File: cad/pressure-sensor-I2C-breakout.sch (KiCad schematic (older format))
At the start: 9 parts, among them P1 CONN_4, P2 CONN_4, U1 MPXV-PRESSURE-SENSOR, U2 LTC2483

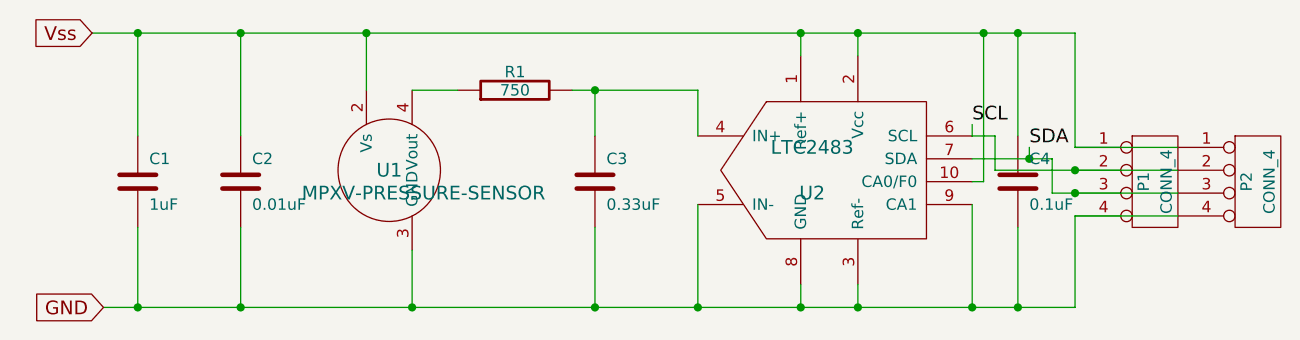
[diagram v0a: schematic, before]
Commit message: Fixing broken heater logic. Clunky but obvious code
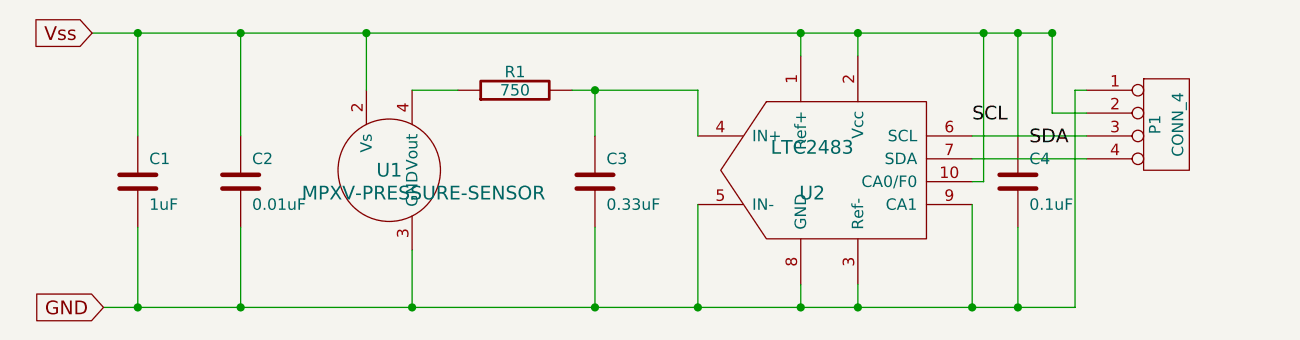
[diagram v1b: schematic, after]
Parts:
- removed P2: CONN_4, symbol CONN_4
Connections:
- net GND: now also P1.1 (P1); no longer P1.4 (P4)
- net SCL: no longer P1.2 (P2), U2.6 (SCL)
- net SDA: no longer P1.3 (P3), U2.7 (SDA)
- net Vss: now also P1.2 (P2); no longer P1.1 (P1)
- new net: P1.3 (P3), U2.6 (SCL)
- new net: P1.4 (P4), U2.7 (SDA)
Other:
- moved on the sheet: P1
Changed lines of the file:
@@
-EESchema Schematic File Version 2  date Mon 24 Feb 2014 17:03:24 NZDT
+EESchema Schematic File Version 2
 LIBS:power
 LIBS:device
@@
 LIBS:valves
 LIBS:state-machine-library_kicad
-EELAYER 25  0
+LIBS:pressure-sensor-I2C-breakout-cache
+EELAYER 27 0
 EELAYER END
-$Descr A4 11700 8267
+$Descr A4 11693 8268
 encoding utf-8
 Sheet 1 1
 Title ""
-Date "23 feb 2014"
+Date "20 may 2014"
 Rev ""
 Comp ""
@@
 Wire Wire Line
 	7250 2850 7200 2850
-Connection ~ 7450 2750
-Wire Wire Line
-	7450 2700 7450 2750
 Connection ~ 3550 3400
 Wire Wire Line
@@
 	4750 2450 4950 2450
 Wire Wire Line
-	8100 2900 7550 2900
-Wire Wire Line
-	7550 2900 7550 2750
-Wire Wire Line
-	7550 2750 7200 2750
+	7200 2750 7700 2750
 Connection ~ 6700 2200
 Wire Wire Line
-	6700 2300 6700 2200
+	6700 2200 6700 2300
 Connection ~ 6700 3400
 Wire Wire Line
@@
 Wire Wire Line
 	6000 2950 6000 3400
-Wire Wire Line
-	8100 2700 7650 2700
-Connection ~ 7650 2900
 Connection ~ 7400 2200
 Wire Wire Line
@@
 Connection ~ 4000 2200
 Wire Wire Line
-	4000 2650 4000 2200
+	4000 2200 4000 2650
 Connection ~ 4000 3400
 Wire Wire Line
@@
 Wire Wire Line
 	3550 3400 3550 3050
-Wire Wire Line
-	7650 3400 7650 3000
-Wire Wire Line
-	7650 2700 7650 2200
 Wire Wire Line
 	3550 2200 3550 2650
@@
 Connection ~ 7400 3400
 Wire Wire Line
-	7650 3000 8100 3000
-Connection ~ 7650 2800
-Wire Wire Line
 	5450 2450 6000 2450
 Wire Wire Line
@@
 Connection ~ 6450 3400
 Wire Wire Line
-	6450 2300 6450 2200
+	6450 2200 6450 2300
 Connection ~ 6450 2200
 Wire Wire Line
-	7300 2650 7200 2650
-Wire Wire Line
-	7300 2650 7300 2800
-Wire Wire Line
-	7300 2800 8100 2800
+	7200 2650 7700 2650
 Wire Wire Line
 	4550 2200 4550 2450
 Wire Wire Line
 	4750 3150 4750 3400
-Wire Wire Line
-	7650 2200 3350 2200
 Connection ~ 3550 2200
-Wire Wire Line
-	7200 2650 7200 2600
 Wire Wire Line
 	7200 2950 7200 3400
@@
 GND
 $Comp
-L CONN_4 P2
-U 1 1 530999F2
-P 8450 2850
-F 0 "P2" V 8400 2850 50  0000 C CNN
-F 1 "CONN_4" V 8500 2850 50  0000 C CNN
-	1    8450 2850
-	1    0    0    -1
-$EndComp
-$Comp
 L CONN_4 P1
 U 1 1 530997F9
-P 8000 2850
-F 0 "P1" V 7950 2850 50  0000 C CNN
-F 1 "CONN_4" V 8050 2850 50  0000 C CNN
-	1    8000 2850
+P 8050 2600
+F 0 "P1" V 8000 2600 50  0000 C CNN
+F 1 "CONN_4" V 8100 2600 50  0000 C CNN
+F 2 "" H 8050 2600 60  0001 C CNN
+F 3 "" H 8050 2600 60  0001 C CNN
+	1    8050 2600
 	1    0    0    -1
 $EndComp
@@
 F 0 "C4" H 7450 2950 50  0000 L CNN
 F 1 "0.1uF" H 7450 2750 50  0000 L CNN
+F 2 "" H 7400 2850 60  0001 C CNN
+F 3 "" H 7400 2850 60  0001 C CNN
 	1    7400 2850
 	1    0    0    -1
@@
 F 0 "C3" H 5600 2950 50  0000 L CNN
 F 1 "0.33uF" H 5600 2750 50  0000 L CNN
+F 2 "" H 5550 2850 60  0001 C CNN
+F 3 "" H 5550 2850 60  0001 C CNN
 	1    5550 2850
 	1    0    0    -1
@@
 F 0 "C1" H 3600 2950 50  0000 L CNN
 F 1 "1uF" H 3600 2750 50  0000 L CNN
+F 2 "" H 3550 2850 60  0001 C CNN
+F 3 "" H 3550 2850 60  0001 C CNN
 	1    3550 2850
 	1    0    0    -1
@@
 F 0 "C2" H 4050 2950 50  0000 L CNN
 F 1 "0.01uF" H 4050 2750 50  0000 L CNN
+F 2 "" H 4000 2850 60  0001 C CNN
+F 3 "" H 4000 2850 60  0001 C CNN
 	1    4000 2850
 	1    0    0    -1
@@
 F 0 "R1" V 5280 2450 50  0000 C CNN
 F 1 "750" V 5200 2450 50  0000 C CNN
+F 2 "" H 5200 2450 60  0001 C CNN
+F 3 "" H 5200 2450 60  0001 C CNN
 	1    5200 2450
 	0    -1   -1   0
@@
 F 0 "U2" H 6500 2700 60  0000 C CNN
 F 1 "LTC2483" H 6500 2900 60  0000 C CNN
+F 2 "" H 6500 2800 60  0001 C CNN
+F 3 "" H 6500 2800 60  0001 C CNN
 	1    6500 2800
 	1    0    0    -1
@@
 F 0 "U1" H 4650 2800 60  0000 C CNN
 F 1 "MPXV-PRESSURE-SENSOR" H 4800 2700 60  0000 C CNN
+F 2 "" H 4650 2800 60  0001 C CNN
+F 3 "" H 4650 2800 60  0001 C CNN
 	1    4650 2800
 	1    0    0    -1
 $EndComp
+Wire Wire Line
+	7650 3400 7650 2450
+Wire Wire Line
+	7650 2450 7700 2450
+Wire Wire Line
+	7550 2200 7550 2550
+Wire Wire Line
+	7550 2550 7700 2550
+Connection ~ 7550 2200
+Wire Wire Line
+	3350 2200 7550 2200
 $EndSCHEMATC
